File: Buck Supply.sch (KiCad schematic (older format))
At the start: 1 part

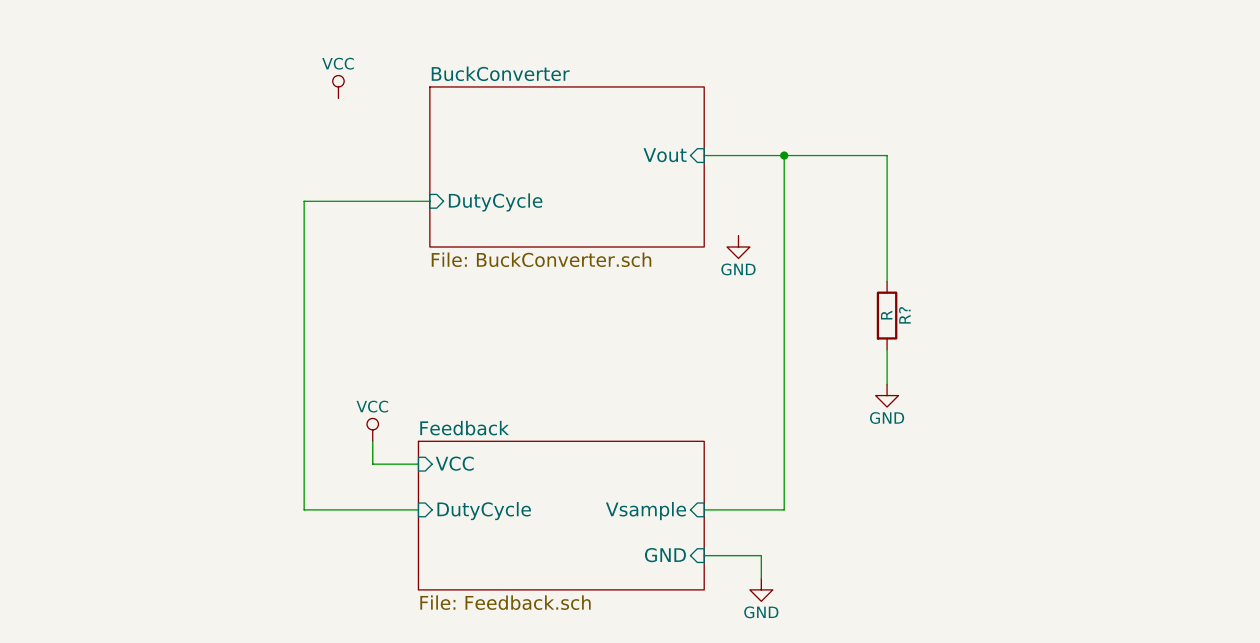
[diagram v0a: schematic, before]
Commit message: Added the basic Buck Schematic with the IRL2004
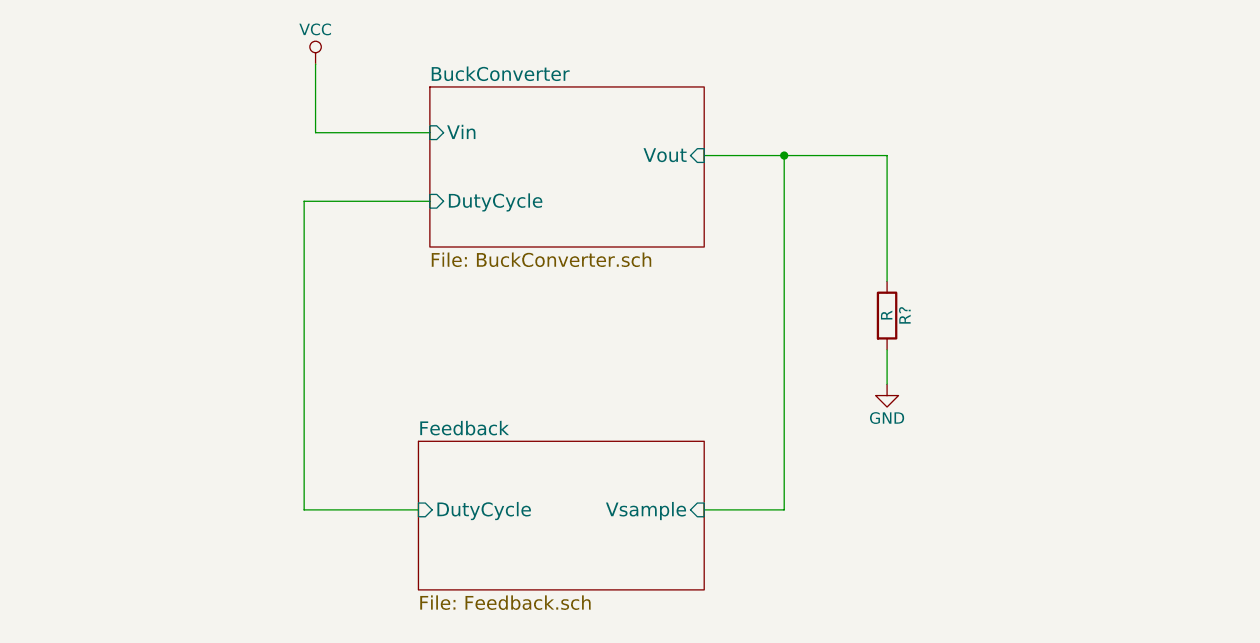
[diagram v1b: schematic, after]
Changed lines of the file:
@@
 LIBS:valves
 LIBS:Buck Supply-cache
+LIBS:ir
 EELAYER 25 0
 EELAYER END
@@
 F2 "Vsample" I R 4700 4300 60
 F3 "DutyCycle" I L 3450 4300 60
-F4 "GND" I R 4700 4500 60
-F5 "VCC" I L 3450 4100 60
 $EndSheet
 $Sheet
@@
 F2 "DutyCycle" I L 3500 2950 60
 F3 "Vout" I R 4700 2750 60
+F4 "Vin" I L 3500 2650 60
 $EndSheet
 Wire Wire Line
@@
 	2950 2950 3500 2950
 Wire Wire Line
-	4700 2750 5050 2750
-Wire Wire Line
-	5050 2750 5500 2750
+	4700 2750 5500 2750
 Wire Wire Line
 	5500 2750 5500 3300
@@
 $Comp
 L VCC #PWR?
-U 1 1 58B684ED
-P 3250 4000
-F 0 "#PWR?" H 3250 3850 50  0001 C CNN
-F 1 "VCC" H 3250 4150 50  0000 C CNN
-F 2 "" H 3250 4000 50  0000 C CNN
-F 3 "" H 3250 4000 50  0000 C CNN
-	1    3250 4000
+U 1 1 58B71B6E
+P 3000 2350
+F 0 "#PWR?" H 3000 2200 50  0001 C CNN
+F 1 "VCC" H 3000 2500 50  0000 C CNN
+F 2 "" H 3000 2350 50  0000 C CNN
+F 3 "" H 3000 2350 50  0000 C CNN
+	1    3000 2350
 	1    0    0    -1
 $EndComp
 Wire Wire Line
-	3450 4100 3250 4100
+	3500 2650 3000 2650
 Wire Wire Line
-	3250 4100 3250 4000
-$Comp
-L GND #PWR?
-U 1 1 58B6896E
-P 4950 4600
-F 0 "#PWR?" H 4950 4350 50  0001 C CNN
-F 1 "GND" H 4950 4450 50  0000 C CNN
-F 2 "" H 4950 4600 50  0000 C CNN
-F 3 "" H 4950 4600 50  0000 C CNN
-	1    4950 4600
-	1    0    0    -1
-$EndComp
-Wire Wire Line
-	4700 4500 4950 4500
-Wire Wire Line
-	4950 4500 4950 4600
-$Comp
-L GND #PWR?
-U 1 1 58B6986B
-P 4850 3100
-F 0 "#PWR?" H 4850 2850 50  0001 C CNN
-F 1 "GND" H 4850 2950 50  0000 C CNN
-F 2 "" H 4850 3100 50  0000 C CNN
-F 3 "" H 4850 3100 50  0000 C CNN
-	1    4850 3100
-	1    0    0    -1
-$EndComp
-$Comp
-L VCC #PWR?
-U 1 1 58B698A5
-P 3100 2500
-F 0 "#PWR?" H 3100 2350 50  0001 C CNN
-F 1 "VCC" H 3100 2650 50  0000 C CNN
-F 2 "" H 3100 2500 50  0000 C CNN
-F 3 "" H 3100 2500 50  0000 C CNN
-	1    3100 2500
-	1    0    0    -1
-$EndComp
+	3000 2650 3000 2350
 $EndSCHEMATC

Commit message: Did a whole bunch of layout
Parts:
- added P1: INPUT, Connectors:Banana_Jack_2Pin, symbol CONN_01X02
- added P2: OUTPUT, Connectors:Banana_Jack_2Pin, symbol CONN_01X02
- R1: renamed from R?; value R -> Rload; footprint (none) -> Resistors_THT:Resistor_Horizontal_RM30mm
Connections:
- net BuckConverter/Vout: now also P2.1 (P1)
- net GND: now also P1.2 (P2), P2.2 (P2)
- net VCC: now also P1.1 (P1)
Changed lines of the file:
@@
 	2950 2950 3500 2950
 Wire Wire Line
-	4700 2750 5500 2750
+	4700 2750 6700 2750
 Wire Wire Line
 	5500 2750 5500 3300
 $Comp
-L R R?
+L R R1
 U 1 1 58B6518C
 P 5500 3450
-F 0 "R?" V 5580 3450 50  0000 C CNN
-F 1 "R" V 5500 3450 50  0000 C CNN
-F 2 "" V 5430 3450 50  0000 C CNN
+F 0 "R1" V 5580 3450 50  0000 C CNN
+F 1 "Rload" V 5500 3450 50  0000 C CNN
+F 2 "Resistors_THT:Resistor_Horizontal_RM30mm" V 5430 3450 50  0001 C CNN
 F 3 "" H 5500 3450 50  0000 C CNN
 	1    5500 3450
@@
 $EndComp
 $Comp
-L GND #PWR?
+L GND #PWR01
 U 1 1 58B651EF
 P 5500 3750
-F 0 "#PWR?" H 5500 3500 50  0001 C CNN
+F 0 "#PWR01" H 5500 3500 50  0001 C CNN
 F 1 "GND" H 5500 3600 50  0000 C CNN
 F 2 "" H 5500 3750 50  0000 C CNN
@@
 Connection ~ 5050 2750
 $Comp
-L VCC #PWR?
+L VCC #PWR02
 U 1 1 58B71B6E
 P 3000 2350
-F 0 "#PWR?" H 3000 2200 50  0001 C CNN
+F 0 "#PWR02" H 3000 2200 50  0001 C CNN
 F 1 "VCC" H 3000 2500 50  0000 C CNN
 F 2 "" H 3000 2350 50  0000 C CNN
@@
 Wire Wire Line
 	3000 2650 3000 2350
+$Comp
+L CONN_01X02 P1
+U 1 1 58BB5DA9
+P 1850 2800
+F 0 "P1" H 1850 2950 50  0000 C CNN
+F 1 "INPUT" V 1950 2800 50  0000 C CNN
+F 2 "Connectors:Banana_Jack_2Pin" H 1850 2800 50  0001 C CNN
+F 3 "" H 1850 2800 50  0000 C CNN
+	1    1850 2800
+	-1   0    0    -1
+$EndComp
+$Comp
+L GND #PWR03
+U 1 1 58BB5E71
+P 2200 3000
+F 0 "#PWR03" H 2200 2750 50  0001 C CNN
+F 1 "GND" H 2200 2850 50  0000 C CNN
+F 2 "" H 2200 3000 50  0000 C CNN
+F 3 "" H 2200 3000 50  0000 C CNN
+	1    2200 3000
+	1    0    0    -1
+$EndComp
+$Comp
+L VCC #PWR04
+U 1 1 58BB5EB8
+P 2200 2600
+F 0 "#PWR04" H 2200 2450 50  0001 C CNN
+F 1 "VCC" H 2200 2750 50  0000 C CNN
+F 2 "" H 2200 2600 50  0000 C CNN
+F 3 "" H 2200 2600 50  0000 C CNN
+	1    2200 2600
+	1    0    0    -1
+$EndComp
+Wire Wire Line
+	2050 2750 2200 2750
+Wire Wire Line
+	2200 2750 2200 2600
+Wire Wire Line
+	2050 2850 2200 2850
+Wire Wire Line
+	2200 2850 2200 3000
+$Comp
+L CONN_01X02 P2
+U 1 1 58BB6321
+P 6900 2800
+F 0 "P2" H 6900 2950 50  0000 C CNN
+F 1 "OUTPUT" V 7000 2800 50  0000 C CNN
+F 2 "Connectors:Banana_Jack_2Pin" H 6900 2800 50  0001 C CNN
+F 3 "" H 6900 2800 50  0000 C CNN
+	1    6900 2800
+	1    0    0    -1
+$EndComp
+Connection ~ 5500 2750
+$Comp
+L GND #PWR05
+U 1 1 58BB63C0
+P 6550 2950
+F 0 "#PWR05" H 6550 2700 50  0001 C CNN
+F 1 "GND" H 6550 2800 50  0000 C CNN
+F 2 "" H 6550 2950 50  0000 C CNN
+F 3 "" H 6550 2950 50  0000 C CNN
+	1    6550 2950
+	1    0    0    -1
+$EndComp
+Wire Wire Line
+	6700 2850 6550 2850
+Wire Wire Line
+	6550 2850 6550 2950
 $EndSCHEMATC
